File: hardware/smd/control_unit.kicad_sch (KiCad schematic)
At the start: 26 parts, among them J5 UART, J6 Conn_01x02_Pin, K1 SPST, 5V 72R, 10A 250VAC, Q1 NPN, 40V, 500mA, U5 ESP32-H2, Y1 32MHz ±10ppm CL8pF

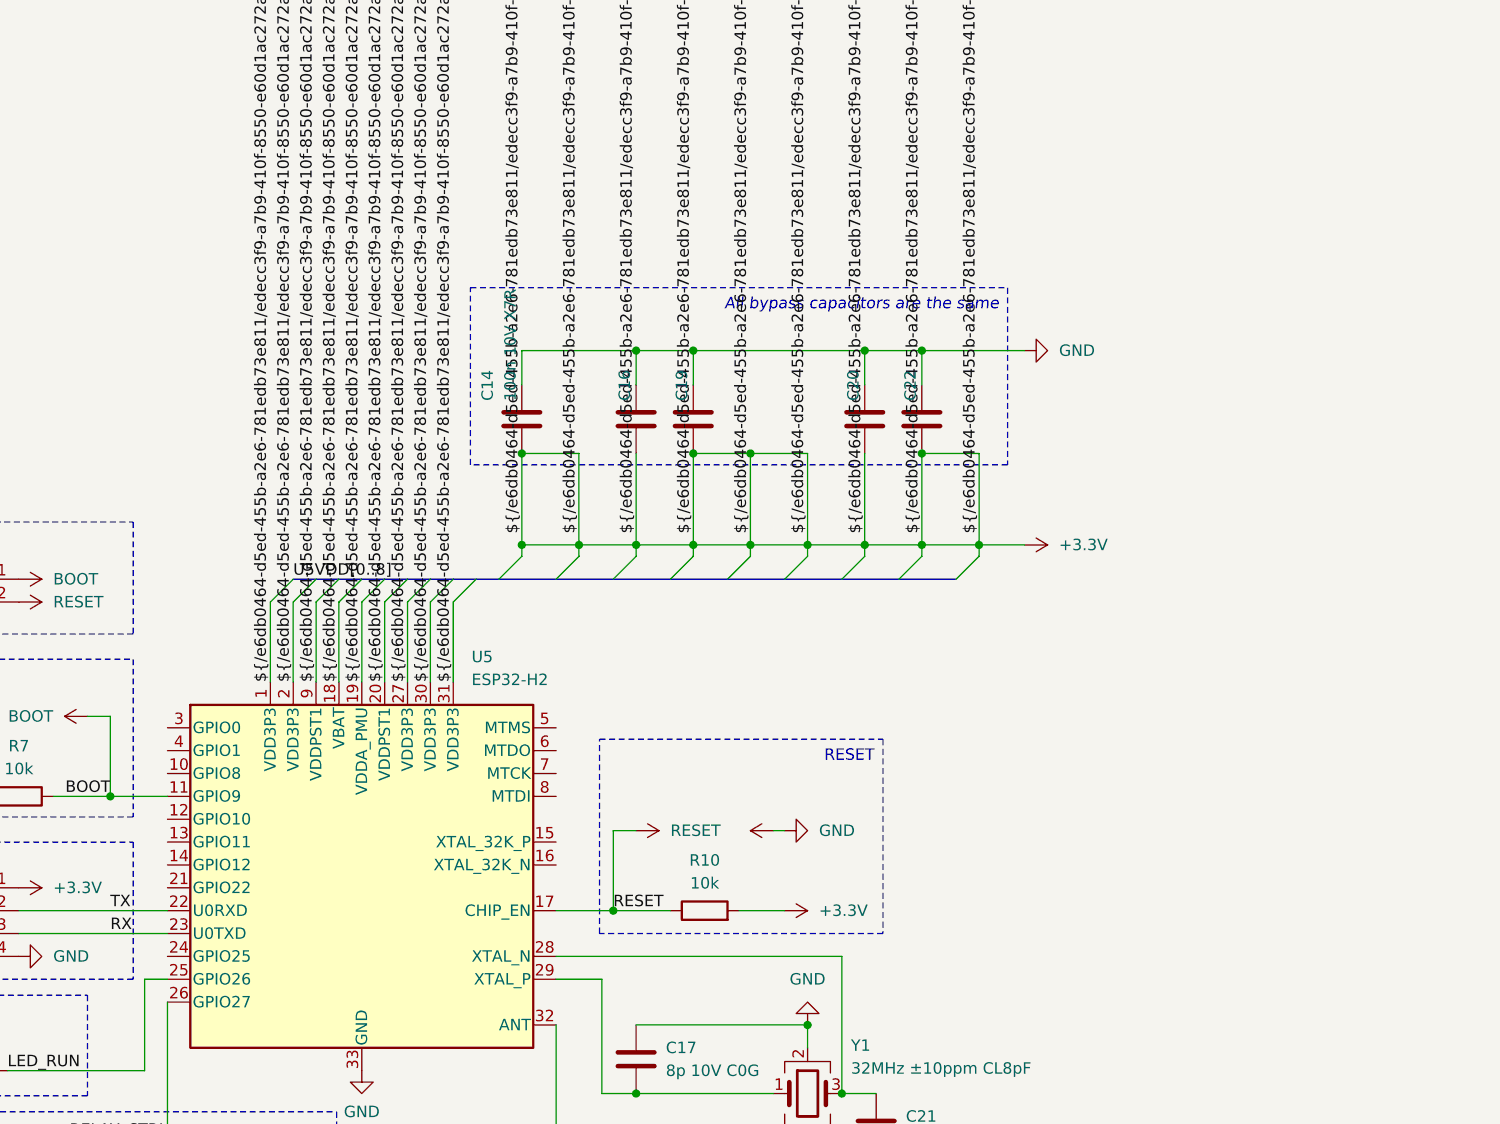
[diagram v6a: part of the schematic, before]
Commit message: Relink symbols and footprints to new lib and fix few errors
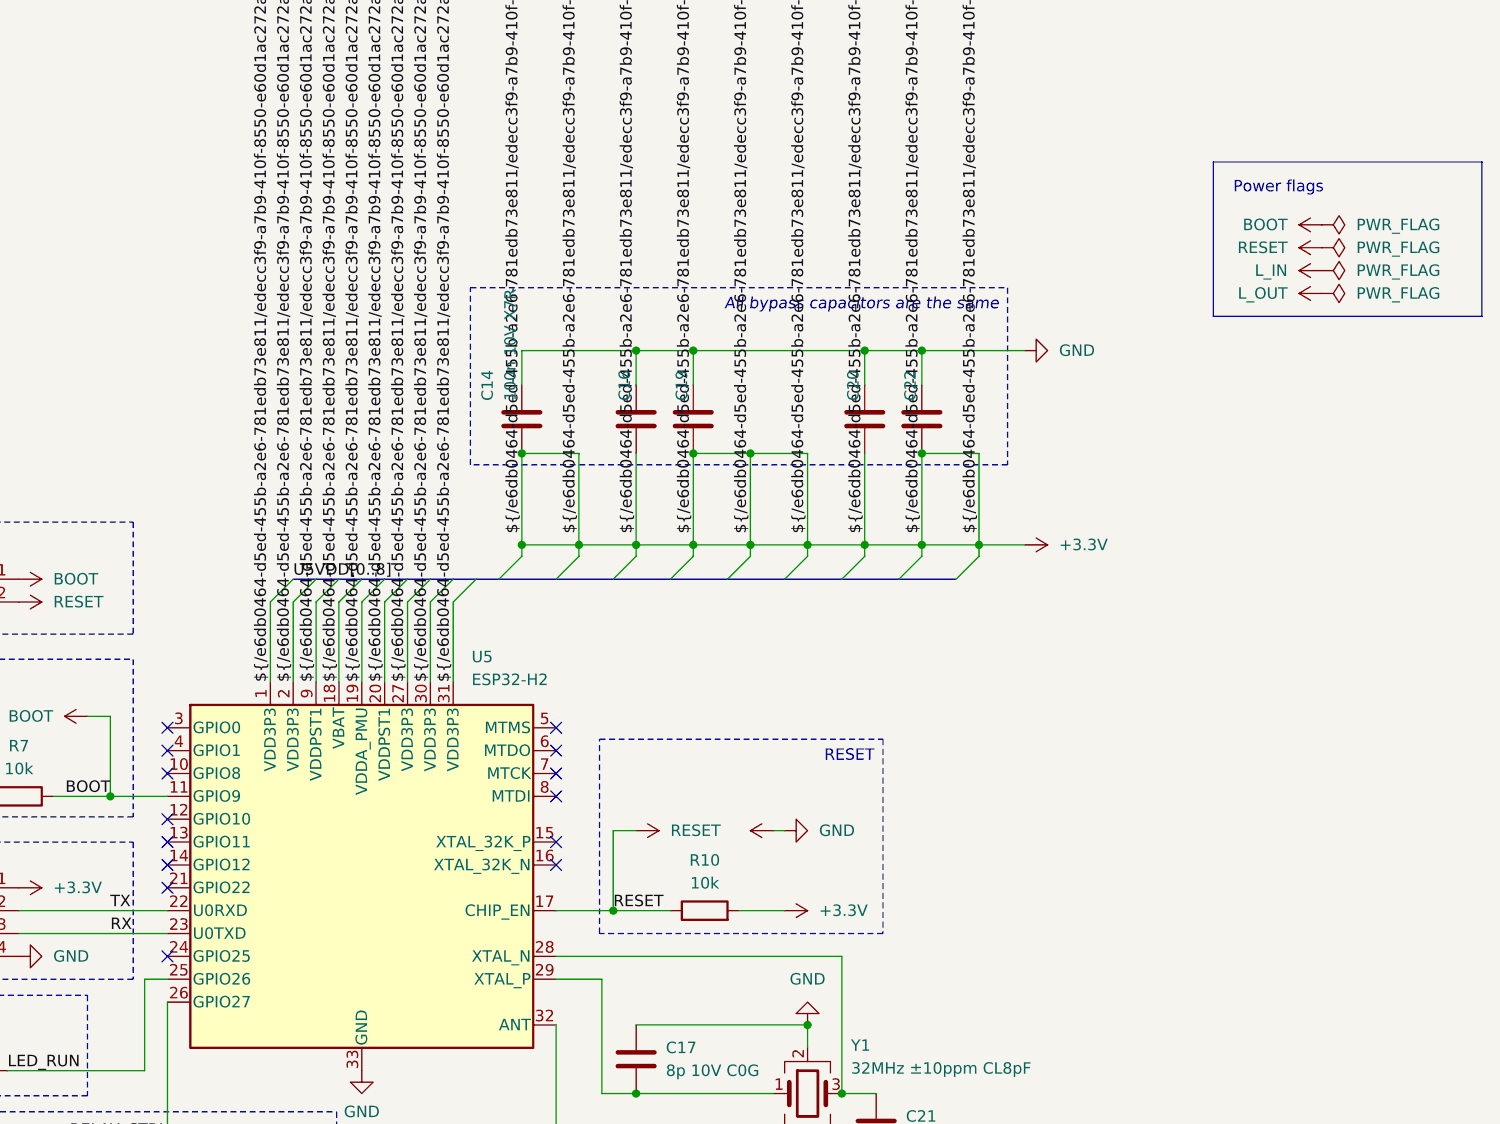
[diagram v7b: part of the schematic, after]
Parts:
- AE1: footprint KiCadX_Antennas_SMD:PCB_antenna_Espressif_2.4GHz_right -> PCM_SKC_Antennas_SMD:Antenna_PCB_Espressif_2.4GHz_Right
- K1: footprint KiCadX_Relays_THT:Relay_SPST_OJ_SH_105HM_000 -> PCM_SKC_Relays_THT:OJ_SH_105HM_SPST
- U5: footprint KiCadX_MCU_Espressif:TQFN_32_1EP_4x4mm_P0.4mm_EP2.4x2.4mm_Compact -> PCM_SKC_MCU_Espressif:TQFN_32_1EP_4x4mm_P0.4mm_EP2.4x2.4mm_Compact
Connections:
- no-connect marks 0 -> 14
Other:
- note added: "Power flags"

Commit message: Fix typo in capacitors for oscillator
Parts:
- C17, C21: value 8p 10V C0G -> 15p 10V C0G
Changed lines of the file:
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@@
 			)
 		)
-		(property "Value" "8p 10V C0G"
+		(property "Value" "15p 10V C0G"
 			(at 188.722 119.38 0)
 			(effects
@@
 			)
 		)
-		(property "Value" "8p 10V C0G"
+		(property "Value" "15p 10V C0G"
 			(at 215.392 127 0)
 			(effects
